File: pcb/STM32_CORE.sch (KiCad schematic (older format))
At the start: 33 parts, among them J11 Conn_01x04, J12 Conn_01x04, J6 Conn_01x14, J7 Conn_01x12, J8 Conn_01x15, SW1 SW_Push, U3 STM32F103C8T6, U4 AMS1117-3.3, Y1 O8M, Y2 O_EPSON_32.768K

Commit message: add capacitor to the main 5V
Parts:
- added C20: CP220uf,50V, Capacitor_SMD:CP_Elec_10x10.5, symbol taobao-cp:CP220uf,50V
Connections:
- wire segments 178 -> 180
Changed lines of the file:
@@
 $EndComp
-Wire Wire Line
-	11400 4800 11400 5000
-Wire Wire Line
-	11400 5000 11550 5000
 Wire Wire Line
 	11550 5000 11550 5150
@@
 L customized_power:+5V #PWR033
 U 1 1 5BCE8D55
-P 11400 4800
-F 0 "#PWR033" H 11400 4650 50  0001 C CNN
-F 1 "+5V" H 11450 5000 50  0000 C CNN
-F 2 "" H 11400 4800 50  0001 C CNN
-F 3 "" H 11400 4800 50  0001 C CNN
-	1    11400 4800
+P 11050 4800
+F 0 "#PWR033" H 11050 4650 50  0001 C CNN
+F 1 "+5V" H 11100 5000 50  0000 C CNN
+F 2 "" H 11050 4800 50  0001 C CNN
+F 3 "" H 11050 4800 50  0001 C CNN
+	1    11050 4800
 	1    0    0    -1
 $EndComp
@@
 	0    1    -1   0
 $EndComp
+$Comp
+L taobao-cp:CP220uf,50V C20
+U 1 1 5BD81A30
+P 11050 5250
+F 0 "C20" H 11138 5296 50  0000 L CNN
+F 1 "CP220uf,50V" H 11138 5205 50  0000 L CNN
+F 2 "Capacitor_SMD:CP_Elec_10x10.5" H 11050 5250 50  0001 C CNN
+F 3 "~" H 11050 5250 50  0001 C CNN
+	1    11050 5250
+	1    0    0    -1
+$EndComp
+Wire Wire Line
+	11050 4800 11050 5000
+Wire Wire Line
+	11050 5000 11550 5000
+Connection ~ 11050 5000
+Wire Wire Line
+	11050 5000 11050 5150
+$Comp
+L power:GND #PWR?
+U 1 1 5BD949F8
+P 11050 5550
+F 0 "#PWR?" H 11050 5300 50  0001 C CNN
+F 1 "GND" H 11055 5377 50  0000 C CNN
+F 2 "" H 11050 5550 50  0001 C CNN
+F 3 "" H 11050 5550 50  0001 C CNN
+	1    11050 5550
+	1    0    0    -1
+$EndComp
+Wire Wire Line
+	11050 5350 11050 5550
 $EndSCHEMATC

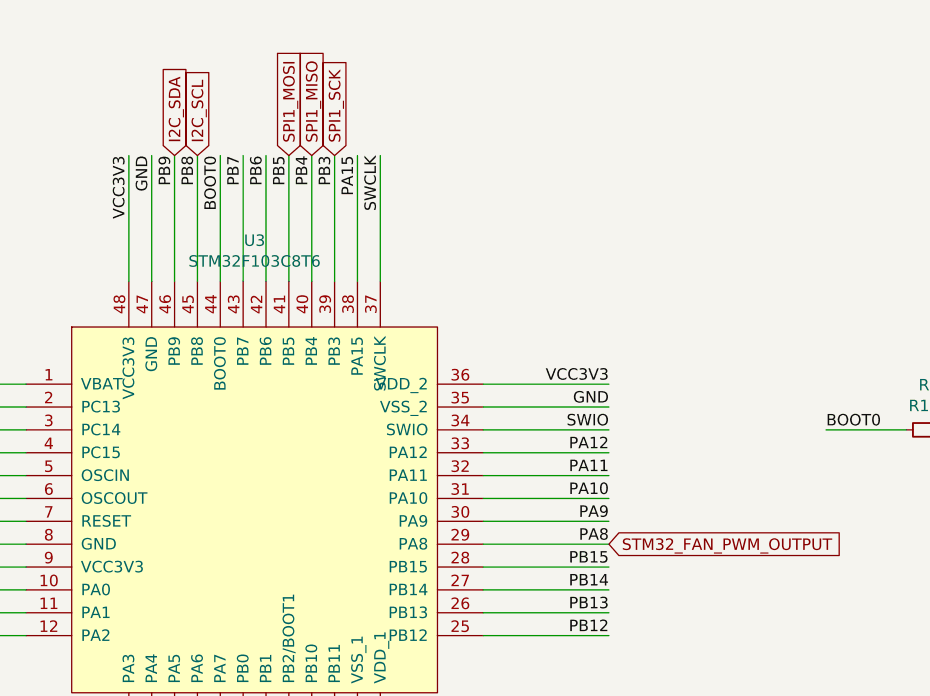
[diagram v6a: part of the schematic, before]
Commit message: update I2C position, SPI position,
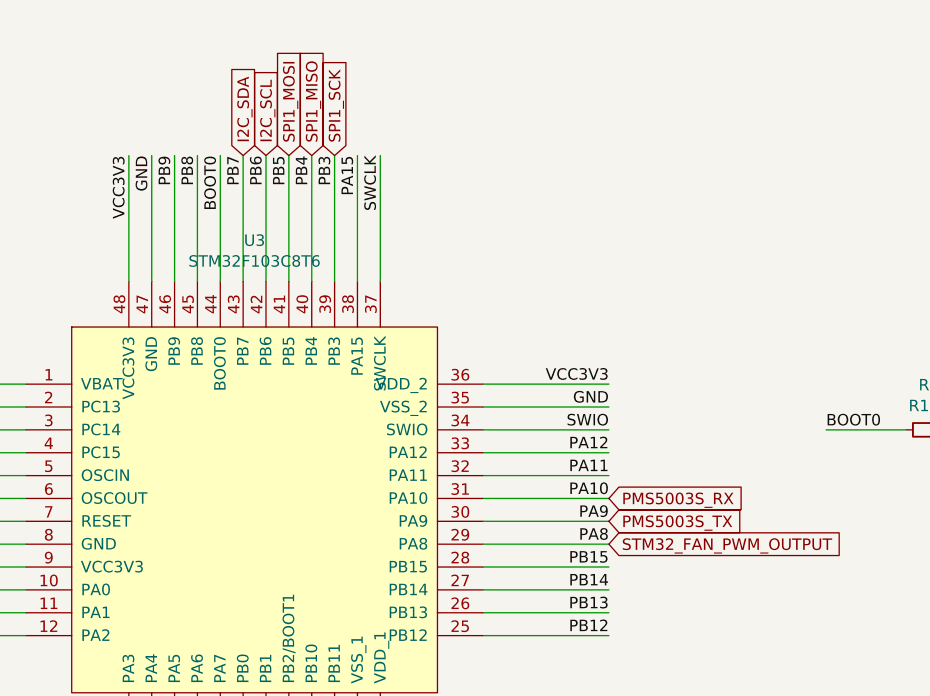
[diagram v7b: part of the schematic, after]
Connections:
- net labels added: PMS5003S_RX, PMS5003S_TX
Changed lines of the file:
@@
 	0    -1   -1   0
 $EndComp
-Text GLabel 8100 1650 1    50   Input ~ 0
+Text GLabel 8400 1650 1    50   Input ~ 0
 I2C_SDA
-Text GLabel 8200 1650 1    50   Input ~ 0
+Text GLabel 8500 1650 1    50   Input ~ 0
 I2C_SCL
 Text GLabel 8600 1650 1    50   Input ~ 0
@@
 	11050 5000 11050 5150
 $Comp
-L power:GND #PWR?
+L power:GND #PWR0115
 U 1 1 5BD949F8
 P 11050 5550
-F 0 "#PWR?" H 11050 5300 50  0001 C CNN
+F 0 "#PWR0115" H 11050 5300 50  0001 C CNN
 F 1 "GND" H 11055 5377 50  0000 C CNN
 F 2 "" H 11050 5550 50  0001 C CNN
@@
 Wire Wire Line
 	11050 5350 11050 5550
+Text GLabel 10000 3150 2    50   Input ~ 0
+PMS5003S_RX
+Text GLabel 10000 3250 2    50   Input ~ 0
+PMS5003S_TX
 $EndSCHEMATC

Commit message: update VBAT pin with 3V3,
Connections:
- net labels added: VDD_1, VDD_2, VSS_1, VSS_2
- wire segments 180 -> 191
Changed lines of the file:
@@
 	8800 4750 8800 4200
 Text Label 8900 4750 1    50   ~ 0
-GND
+VSS_1
 Wire Wire Line
 	8900 4750 8900 4200
 Text Label 9000 4750 1    50   ~ 0
-VCC3V3
+VDD_1
 Wire Wire Line
 	9000 4750 9000 4200
@@
 	10000 2850 9450 2850
 Text Label 10000 2750 2    50   ~ 0
-GND
+VSS_2
 Wire Wire Line
 	10000 2750 9450 2750
 Text Label 10000 2650 2    50   ~ 0
-VCC3V3
+VDD_2
 Wire Wire Line
 	10000 2650 9450 2650
@@
 	1    0    0    1
 $EndComp
-Text Label 5600 1700 1    50   ~ 0
+Text Label 6550 1250 2    50   ~ 0
 VCC3V3
 Wire Wire Line
-	5600 1300 5600 1700
+	6100 1100 6100 1250
 $Comp
 L Device:Jumper_NO_Small JP1
@@
 L power:+3V3 #PWR024
 U 1 1 5BCAD5BF
-P 5600 1300
-F 0 "#PWR024" H 5600 1150 50  0001 C CNN
-F 1 "+3V3" H 5650 1500 50  0000 C CNN
-F 2 "" H 5600 1300 50  0001 C CNN
-F 3 "" H 5600 1300 50  0001 C CNN
-	1    5600 1300
+P 6100 1100
+F 0 "#PWR024" H 6100 950 50  0001 C CNN
+F 1 "+3V3" H 6150 1300 50  0000 C CNN
+F 2 "" H 6100 1100 50  0001 C CNN
+F 3 "" H 6100 1100 50  0001 C CNN
+	1    6100 1100
 	1    0    0    -1
 $EndComp
@@
 Text GLabel 10000 3250 2    50   Input ~ 0
 PMS5003S_TX
+Text Label 6550 1400 2    50   ~ 0
+VBAT
+Text Label 6550 1500 2    50   ~ 0
+VDD_2
+Text Label 6550 1600 2    50   ~ 0
+VDD_1
+Wire Wire Line
+	6550 1250 6100 1250
+Connection ~ 6100 1250
+Wire Wire Line
+	6100 1400 6550 1400
+Wire Wire Line
+	6100 1250 6100 1400
+Wire Wire Line
+	6550 1600 6100 1600
+Wire Wire Line
+	6100 1600 6100 1500
+Connection ~ 6100 1400
+Wire Wire Line
+	6550 1500 6100 1500
+Connection ~ 6100 1500
+Wire Wire Line
+	6100 1500 6100 1400
+$Comp
+L power:GND #PWR?
+U 1 1 5BDB5D1B
+P 6100 2300
+F 0 "#PWR?" H 6100 2050 50  0001 C CNN
+F 1 "GND" H 6105 2127 50  0000 C CNN
+F 2 "" H 6100 2300 50  0001 C CNN
+F 3 "" H 6100 2300 50  0001 C CNN
+	1    6100 2300
+	1    0    0    -1
+$EndComp
+Text Label 6550 2000 2    50   ~ 0
+VSS_2
+Text Label 6550 2100 2    50   ~ 0
+VSS_1
+Wire Wire Line
+	6100 2300 6100 2100
+Wire Wire Line
+	6100 2000 6550 2000
+Wire Wire Line
+	6550 2100 6100 2100
+Connection ~ 6100 2100
+Wire Wire Line
+	6100 2100 6100 2000
 $EndSCHEMATC
